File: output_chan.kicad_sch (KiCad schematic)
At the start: 12 parts, among them U5 MAX14917AFM+

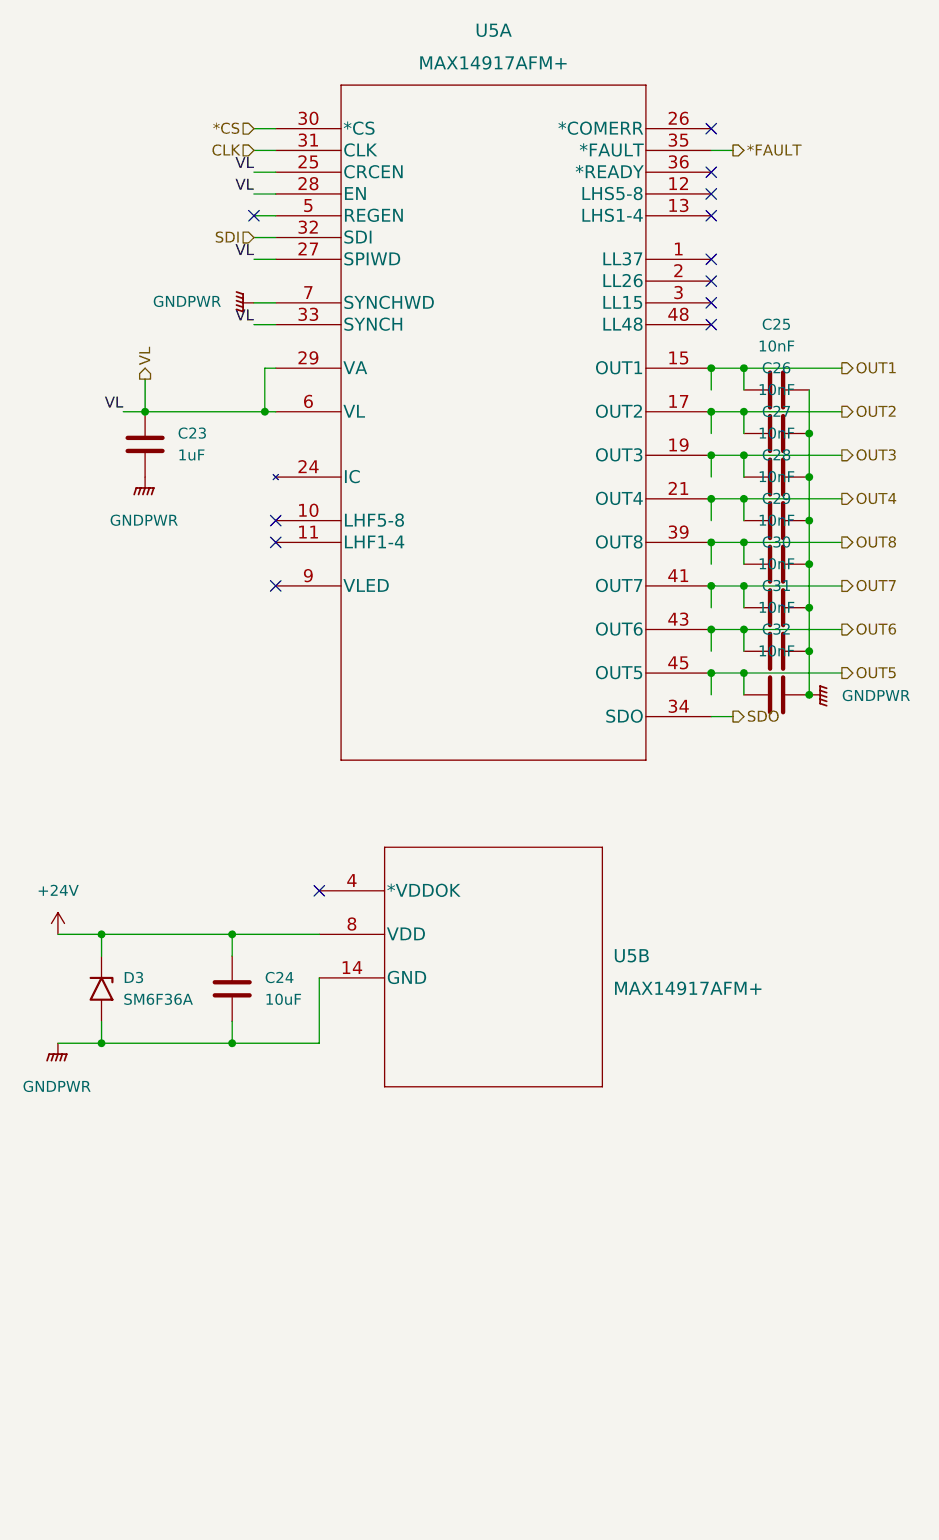
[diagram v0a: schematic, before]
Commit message: Common power stage for field IO
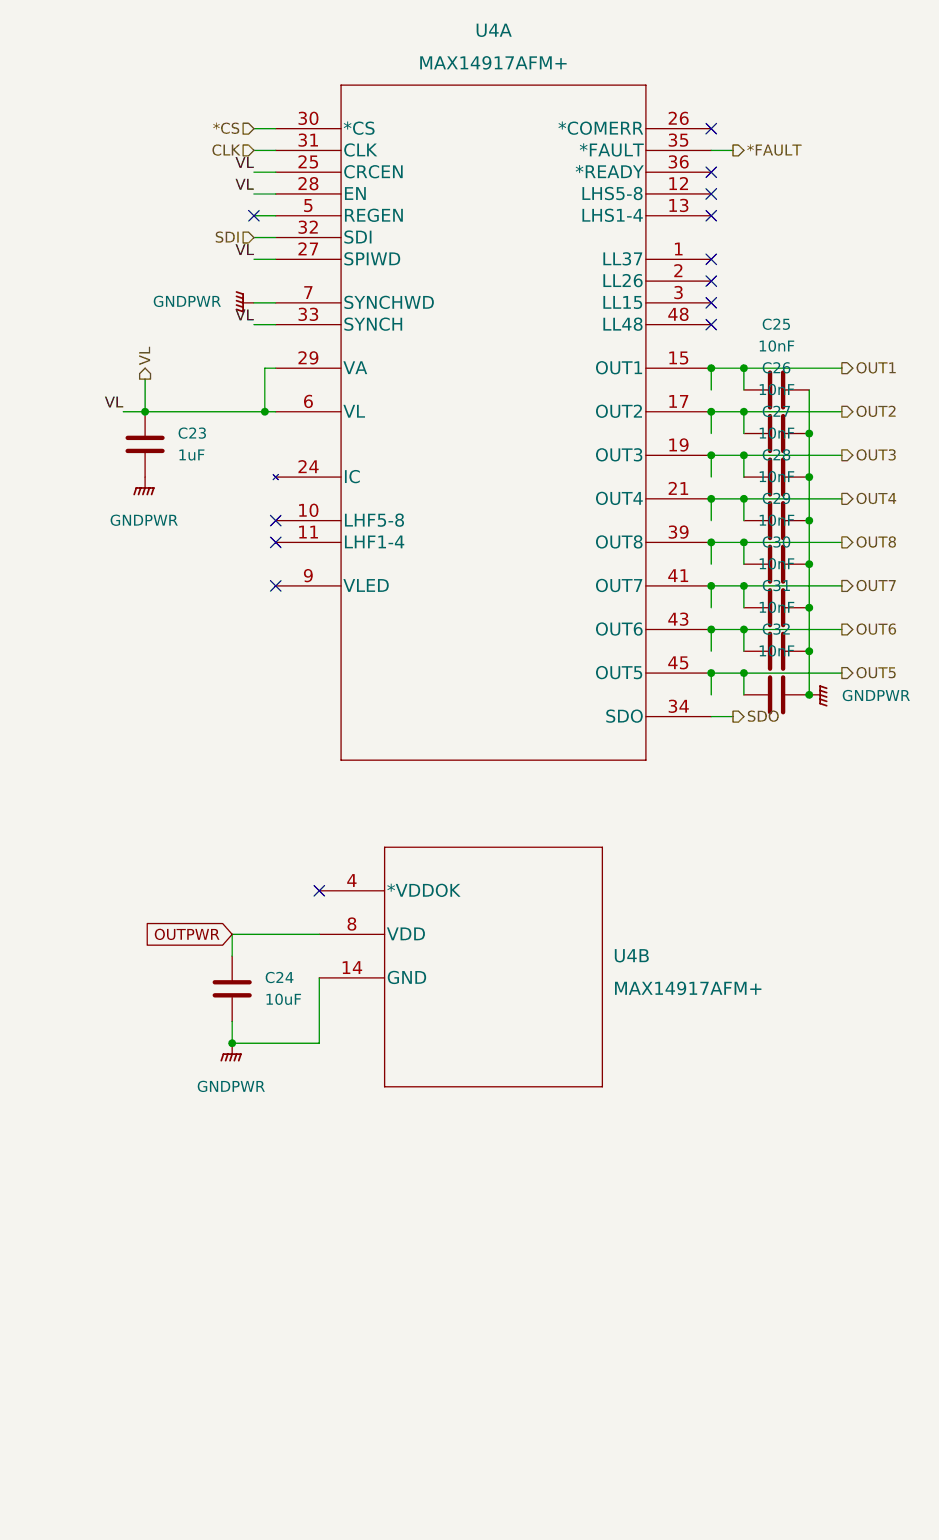
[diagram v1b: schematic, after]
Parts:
- removed D3: SM6F36A, Diode_SMD:D_SMB, symbol Diode:SM6T36A
- renumbered U5 to U4
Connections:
- net +24V renamed OUTPWR
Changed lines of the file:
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@@
   (junction (at 177.8 81.28) (diameter 0) (color 0 0 0 0)
   )
-  (junction (at 106.68 149.86) (diameter 0) (color 0 0 0 0)
-  )
-  (junction (at 121.92 137.16) (diameter 0) (color 0 0 0 0)
-  )
   (junction (at 177.8 96.52) (diameter 0) (color 0 0 0 0)
   )
@@
   (junction (at 189.23 88.9) (diameter 0) (color 0 0 0 0)
   )
-  (junction (at 106.68 137.16) (diameter 0) (color 0 0 0 0)
-  )
   (junction (at 181.61 91.44) (diameter 0) (color 0 0 0 0)
   )
@@
   (junction (at 125.73 76.2) (diameter 0) (color 0 0 0 0)
   )
+  (junction (at 189.23 93.98) (diameter 0) (color 0 0 0 0)
+  )
+  (junction (at 111.76 76.2) (diameter 0) (color 0 0 0 0)
+  )
+  (junction (at 181.61 106.68) (diameter 0) (color 0 0 0 0)
+  )
+  (junction (at 177.8 71.12) (diameter 0) (color 0 0 0 0)
+  )
   (junction (at 121.92 149.86) (diameter 0) (color 0 0 0 0)
-  )
-  (junction (at 189.23 93.98) (diameter 0) (color 0 0 0 0)
-  )
-  (junction (at 111.76 76.2) (diameter 0) (color 0 0 0 0)
-  )
-  (junction (at 181.61 106.68) (diameter 0) (color 0 0 0 0)
-  )
-  (junction (at 177.8 71.12) (diameter 0) (color 0 0 0 0)
   )
   (junction (at 181.61 86.36) (diameter 0) (color 0 0 0 0)
@@
     (stroke (width 0) (type default) (color 0 0 0 0))
   )
-  (wire (pts (xy 106.68 149.86) (xy 121.92 149.86))
-    (stroke (width 0) (type default) (color 0 0 0 0))
-  )
   (wire (pts (xy 125.73 71.12) (xy 125.73 76.2))
     (stroke (width 0) (type default) (color 0 0 0 0))
@@
     (stroke (width 0) (type default) (color 0 0 0 0))
   )
+  (wire (pts (xy 181.61 71.12) (xy 181.61 73.66))
+    (stroke (width 0) (type default) (color 0 0 0 0))
+  )
+  (wire (pts (xy 177.8 91.44) (xy 177.8 93.98))
+    (stroke (width 0) (type default) (color 0 0 0 0))
+  )
   (wire (pts (xy 121.92 149.86) (xy 132.08 149.86))
     (stroke (width 0) (type default) (color 0 0 0 0))
   )
-  (wire (pts (xy 181.61 71.12) (xy 181.61 73.66))
-    (stroke (width 0) (type default) (color 0 0 0 0))
-  )
-  (wire (pts (xy 177.8 91.44) (xy 177.8 93.98))
-    (stroke (width 0) (type default) (color 0 0 0 0))
-  )
   (wire (pts (xy 189.23 104.14) (xy 189.23 109.22))
     (stroke (width 0) (type default) (color 0 0 0 0))
   )
-  (wire (pts (xy 101.6 149.86) (xy 106.68 149.86))
-    (stroke (width 0) (type default) (color 0 0 0 0))
-  )
   (wire (pts (xy 181.61 91.44) (xy 193.04 91.44))
     (stroke (width 0) (type default) (color 0 0 0 0))
@@
     (stroke (width 0) (type default) (color 0 0 0 0))
   )
-  (wire (pts (xy 106.68 147.32) (xy 106.68 149.86))
-    (stroke (width 0) (type default) (color 0 0 0 0))
-  )
   (wire (pts (xy 127 71.12) (xy 125.73 71.12))
     (stroke (width 0) (type default) (color 0 0 0 0))
@@
     (stroke (width 0) (type default) (color 0 0 0 0))
   )
-  (wire (pts (xy 106.68 137.16) (xy 121.92 137.16))
-    (stroke (width 0) (type default) (color 0 0 0 0))
-  )
   (wire (pts (xy 111.76 76.2) (xy 125.73 76.2))
     (stroke (width 0) (type default) (color 0 0 0 0))
   )
   (wire (pts (xy 121.92 137.16) (xy 121.92 139.7))
-    (stroke (width 0) (type default) (color 0 0 0 0))
-  )
-  (wire (pts (xy 101.6 137.16) (xy 106.68 137.16))
-    (stroke (width 0) (type default) (color 0 0 0 0))
-  )
-  (wire (pts (xy 106.68 137.16) (xy 106.68 139.7))
     (stroke (width 0) (type default) (color 0 0 0 0))
   )
@@
     (effects (font (size 1.27 1.27)) (justify right bottom))
   )
+  (global_label "OUTPWR" (shape input) (at 121.92 137.16 180) (fields_autoplaced)
+    (effects (font (size 1.27 1.27)) (justify right))
+    (property "Intersheet References" "${INTERSHEET_REFS}" (id 0) (at 111.8869 137.0806 0)
+      (effects (font (size 1.27 1.27)) (justify right) hide)
+    )
+  )
   (hierarchical_label "OUT5" (shape output) (at 193.04 106.68 0)
     (effects (font (size 1.27 1.27)) (justify left))
@@
   (symbol (lib_id "power:GNDPWR") (at 189.23 109.22 90) (unit 1)
     (in_bom yes) (on_board yes) (fields_autoplaced)
-    (property "Reference" "#PWR020" (id 0) (at 194.31 109.22 0)
+    (property "Reference" "#PWR023" (id 0) (at 194.31 109.22 0)
       (effects (font (size 1.27 1.27)) hide)
     )
@@
   (symbol (lib_id "power:GNDPWR") (at 111.76 83.82 0) (unit 1)
     (in_bom yes) (on_board yes) (fields_autoplaced)
-    (property "Reference" "#PWR019" (id 0) (at 111.76 88.9 0)
+    (property "Reference" "#PWR020" (id 0) (at 111.76 88.9 0)
       (effects (font (size 1.27 1.27)) hide)
     )
@@
   (symbol (lib_id "Maxim industrial IO:MAX14917AFM+") (at 127 43.18 0) (unit 1)
     (in_bom yes) (on_board yes) (fields_autoplaced)
-    (property "Reference" "U5" (id 0) (at 152.4 31.75 0)
+    (property "Reference" "U4" (id 0) (at 152.4 31.75 0)
       (effects (font (size 1.524 1.524)))
     )
@@
   (symbol (lib_id "power:GNDPWR") (at 124.46 63.5 270) (unit 1)
     (in_bom yes) (on_board yes) (fields_autoplaced)
-    (property "Reference" "#PWR0111" (id 0) (at 119.38 63.5 0)
+    (property "Reference" "#PWR022" (id 0) (at 119.38 63.5 0)
       (effects (font (size 1.27 1.27)) hide)
     )
@@
   (symbol (lib_id "Maxim industrial IO:MAX14917AFM+") (at 132.08 132.08 0) (unit 2)
     (in_bom yes) (on_board yes) (fields_autoplaced)
-    (property "Reference" "U5" (id 0) (at 166.37 139.7 0)
+    (property "Reference" "U4" (id 0) (at 166.37 139.7 0)
       (effects (font (size 1.524 1.524)) (justify left))
     )
@@
     (pin "2")
   )
-  (symbol (lib_id "power:+24V") (at 101.6 137.16 0) (unit 1)
-    (in_bom yes) (on_board yes)
-    (property "Reference" "#PWR017" (id 0) (at 101.6 140.97 0)
-      (effects (font (size 1.27 1.27)) hide)
-    )
-    (property "Value" "+24V" (id 1) (at 101.6 132.08 0))
-    (property "Footprint" "" (id 2) (at 101.6 137.16 0)
-      (effects (font (size 1.27 1.27)) hide)
-    )
-    (property "Datasheet" "" (id 3) (at 101.6 137.16 0)
-      (effects (font (size 1.27 1.27)) hide)
-    )
-    (pin "1")
-  )
   (symbol (lib_id "Device:C") (at 185.42 73.66 90) (unit 1)
     (in_bom yes) (on_board yes) (fields_autoplaced)
@@
     (pin "2")
   )
-  (symbol (lib_id "power:GNDPWR") (at 101.6 149.86 0) (unit 1)
-    (in_bom yes) (on_board yes) (fields_autoplaced)
-    (property "Reference" "#PWR018" (id 0) (at 101.6 154.94 0)
-      (effects (font (size 1.27 1.27)) hide)
-    )
-    (property "Value" "GNDPWR" (id 1) (at 101.473 154.94 0))
-    (property "Footprint" "" (id 2) (at 101.6 151.13 0)
-      (effects (font (size 1.27 1.27)) hide)
-    )
-    (property "Datasheet" "" (id 3) (at 101.6 151.13 0)
+  (symbol (lib_id "power:GNDPWR") (at 121.92 149.86 0) (unit 1)
+    (in_bom yes) (on_board yes) (fields_autoplaced)
+    (property "Reference" "#PWR021" (id 0) (at 121.92 154.94 0)
+      (effects (font (size 1.27 1.27)) hide)
+    )
+    (property "Value" "GNDPWR" (id 1) (at 121.793 154.94 0))
+    (property "Footprint" "" (id 2) (at 121.92 151.13 0)
+      (effects (font (size 1.27 1.27)) hide)
+    )
+    (property "Datasheet" "" (id 3) (at 121.92 151.13 0)
       (effects (font (size 1.27 1.27)) hide)
     )
@@
       (effects (font (size 1.27 1.27)) hide)
     )
-    (pin "1")
-    (pin "2")
-  )
-  (symbol (lib_id "Diode:SM6T36A") (at 106.68 143.51 270) (unit 1)
-    (in_bom yes) (on_board yes) (fields_autoplaced)
-    (property "Reference" "D3" (id 0) (at 109.22 142.2399 90)
-      (effects (font (size 1.27 1.27)) (justify left))
-    )
-    (property "Value" "SM6F36A" (id 1) (at 109.22 144.7799 90)
-      (effects (font (size 1.27 1.27)) (justify left))
-    )
-    (property "Footprint" "Diode_SMD:D_SMB" (id 2) (at 101.6 143.51 0)
-      (effects (font (size 1.27 1.27)) hide)
-    )
-    (property "Datasheet" "https://www.st.com/resource/en/datasheet/sm6t.pdf" (id 3) (at 106.68 142.24 0)
-      (effects (font (size 1.27 1.27)) hide)
-    )

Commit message: fix DRC errors
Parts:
- renumbered C23 to C11, C24 to C12, C25 to C13, C26 to C14, C27 to C15, C28 to C16, C29 to C17, C30 to C18, C31 to C19, C32 to C20, U4 to U2
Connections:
- net GNDPWR: now also U2.5 (REGEN); no longer U2.14 (GND), U2.23 (GND), U2.38 (GND), U2.47 (GND)
- net OUTPWR: now also U2.25 (CRCEN); no longer U2.49 (EPAD), U2.8 (VDD)
- new net: U2.15 (OUT1), U2.16 (OUT1)
- new net: U2.17 (OUT2), U2.18 (OUT2)
- new net: U2.19 (OUT3), U2.20 (OUT3)
- new net: U2.21 (OUT4), U2.22 (OUT4)
- new net: U2.37 (VL), U2.6 (VL)
- new net: U2.39 (OUT8), U2.40 (OUT8)
- new net: U2.41 (OUT7), U2.42 (OUT7)
- new net: U2.43 (OUT6), U2.44 (OUT6)
- new net: U2.45 (OUT5), U2.46 (OUT5)
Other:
- note added: "Ajouter un LED de status ?"
- note added: "Deja une PullUp"
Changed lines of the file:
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@@
     (stroke (width 0) (type default) (color 0 0 0 0))
+  )
+  (text "Deja une PullUp" (at 105.41 67.31 0)
+    (effects (font (size 1.27 1.27) italic) (justify left bottom))
+  )
+  (text "Ajouter un LED de status ?" (at 104.14 133.35 0)
+    (effects (font (size 1.27 1.27) italic) (justify left bottom))
   )
   (label "VL" (at 109.22 76.2 180)
@@
     (effects (font (size 1.27 1.27)) (justify right))
   )
-  (symbol (lib_id "power:GNDPWR") (at 189.23 109.22 90) (unit 1)
+  (symbol (lib_id "power:GNDPWR") (at 189.23 109.22 90)
     (in_bom yes) (on_board yes) (fields_autoplaced)
     (property "Reference" "#PWR023" (id 0) (at 194.31 109.22 0)
@@
     (pin "1")
   )
-  (symbol (lib_id "Device:C") (at 111.76 80.01 0) (unit 1)
-    (in_bom yes) (on_board yes) (fields_autoplaced)
-    (property "Reference" "C23" (id 0) (at 115.57 78.7399 0)
+  (symbol (lib_id "Device:C") (at 111.76 80.01 0)
+    (in_bom yes) (on_board yes) (fields_autoplaced)
+    (property "Reference" "C11" (id 0) (at 115.57 78.7399 0)
       (effects (font (size 1.27 1.27)) (justify left))
     )
@@
     (pin "2")
   )
-  (symbol (lib_id "power:GNDPWR") (at 111.76 83.82 0) (unit 1)
+  (symbol (lib_id "power:GNDPWR") (at 111.76 83.82 0)
     (in_bom yes) (on_board yes) (fields_autoplaced)
     (property "Reference" "#PWR020" (id 0) (at 111.76 88.9 0)
@@
     (pin "1")
   )
-  (symbol (lib_id "Maxim industrial IO:MAX14917AFM+") (at 127 43.18 0) (unit 1)
-    (in_bom yes) (on_board yes) (fields_autoplaced)
-    (property "Reference" "U4" (id 0) (at 152.4 31.75 0)
+  (symbol (lib_id "Maxim industrial IO:MAX14917AFM+") (at 127 43.18 0)
+    (in_bom yes) (on_board yes) (fields_autoplaced)
+    (property "Reference" "U2" (id 0) (at 152.4 31.75 0)
       (effects (font (size 1.524 1.524)))
     )
@@
     (pin "7")
     (pin "9")
-    (pin "14")
-    (pin "23")
-    (pin "38")
-    (pin "4")
-    (pin "47")
-    (pin "49")
-    (pin "8")
-  )
-  (symbol (lib_id "Device:C") (at 185.42 83.82 90) (unit 1)
-    (in_bom yes) (on_board yes) (fields_autoplaced)
-    (property "Reference" "C27" (id 0) (at 185.42 76.2 90))
+  )
+  (symbol (lib_id "Device:C") (at 185.42 83.82 90)
+    (in_bom yes) (on_board yes) (fields_autoplaced)
+    (property "Reference" "C15" (id 0) (at 185.42 76.2 90))
     (property "Value" "10nF" (id 1) (at 185.42 78.74 90))
     (property "Footprint" "Capacitor_SMD:C_0603_1608Metric" (id 2) (at 189.23 82.8548 0)
@@
     (pin "2")
   )
-  (symbol (lib_id "Device:C") (at 185.42 88.9 90) (unit 1)
-    (in_bom yes) (on_board yes) (fields_autoplaced)
-    (property "Reference" "C28" (id 0) (at 185.42 81.28 90))
+  (symbol (lib_id "Device:C") (at 185.42 88.9 90)
+    (in_bom yes) (on_board yes) (fields_autoplaced)
+    (property "Reference" "C16" (id 0) (at 185.42 81.28 90))
     (property "Value" "10nF" (id 1) (at 185.42 83.82 90))
     (property "Footprint" "Capacitor_SMD:C_0603_1608Metric" (id 2) (at 189.23 87.9348 0)
@@
     (pin "2")
   )
-  (symbol (lib_id "Device:C") (at 185.42 78.74 90) (unit 1)
-    (in_bom yes) (on_board yes) (fields_autoplaced)
-    (property "Reference" "C26" (id 0) (at 185.42 71.12 90))
+  (symbol (lib_id "Device:C") (at 185.42 78.74 90)
+    (in_bom yes) (on_board yes) (fields_autoplaced)
+    (property "Reference" "C14" (id 0) (at 185.42 71.12 90))
     (property "Value" "10nF" (id 1) (at 185.42 73.66 90))
     (property "Footprint" "Capacitor_SMD:C_0603_1608Metric" (id 2) (at 189.23 77.7748 0)
@@
     (pin "2")
   )
-  (symbol (lib_id "Device:C") (at 185.42 104.14 90) (unit 1)
-    (in_bom yes) (on_board yes) (fields_autoplaced)
-    (property "Reference" "C31" (id 0) (at 185.42 96.52 90))
+  (symbol (lib_id "Device:C") (at 185.42 104.14 90)
+    (in_bom yes) (on_board yes) (fields_autoplaced)
+    (property "Reference" "C19" (id 0) (at 185.42 96.52 90))
     (property "Value" "10nF" (id 1) (at 185.42 99.06 90))
     (property "Footprint" "Capacitor_SMD:C_0603_1608Metric" (id 2) (at 189.23 103.1748 0)
@@
     (pin "2")
   )
-  (symbol (lib_id "power:GNDPWR") (at 124.46 63.5 270) (unit 1)
+  (symbol (lib_id "power:GNDPWR") (at 124.46 63.5 270)
     (in_bom yes) (on_board yes) (fields_autoplaced)
     (property "Reference" "#PWR022" (id 0) (at 119.38 63.5 0)
@@
     (pin "1")
   )
-  (symbol (lib_id "Maxim industrial IO:MAX14917AFM+") (at 132.08 132.08 0) (unit 2)
-    (in_bom yes) (on_board yes) (fields_autoplaced)
-    (property "Reference" "U4" (id 0) (at 166.37 139.7 0)
+  (symbol (lib_id "Maxim industrial IO:MAX14917AFM+") (at 132.08 132.08 0)
+    (in_bom yes) (on_board yes) (fields_autoplaced)
+    (property "Reference" "U2" (id 0) (at 166.37 139.7 0)
       (effects (font (size 1.524 1.524)) (justify left))
     )
@@
     (pin "7")
     (pin "9")
-    (pin "14")
-    (pin "23")
-    (pin "38")
-    (pin "4")
-    (pin "47")
-    (pin "49")
-    (pin "8")
-  )
-  (symbol (lib_id "Device:C") (at 185.42 93.98 90) (unit 1)
-    (in_bom yes) (on_board yes) (fields_autoplaced)
-    (property "Reference" "C29" (id 0) (at 185.42 86.36 90))
+  )
+  (symbol (lib_id "Device:C") (at 185.42 93.98 90)
+    (in_bom yes) (on_board yes) (fields_autoplaced)
+    (property "Reference" "C17" (id 0) (at 185.42 86.36 90))
     (property "Value" "10nF" (id 1) (at 185.42 88.9 90))
     (property "Footprint" "Capacitor_SMD:C_0603_1608Metric" (id 2) (at 189.23 93.0148 0)
@@
     (pin "2")
   )
-  (symbol (lib_id "Device:C") (at 185.42 73.66 90) (unit 1)
-    (in_bom yes) (on_board yes) (fields_autoplaced)
-    (property "Reference" "C25" (id 0) (at 185.42 66.04 90))
+  (symbol (lib_id "Device:C") (at 185.42 73.66 90)
+    (in_bom yes) (on_board yes) (fields_autoplaced)
+    (property "Reference" "C13" (id 0) (at 185.42 66.04 90))
     (property "Value" "10nF" (id 1) (at 185.42 68.58 90))
     (property "Footprint" "Capacitor_SMD:C_0603_1608Metric" (id 2) (at 189.23 72.6948 0)
@@
     (pin "2")
   )
-  (symbol (lib_id "Device:C") (at 185.42 99.06 90) (unit 1)
-    (in_bom yes) (on_board yes) (fields_autoplaced)
-    (property "Reference" "C30" (id 0) (at 185.42 91.44 90))
+  (symbol (lib_id "Device:C") (at 185.42 99.06 90)
+    (in_bom yes) (on_board yes) (fields_autoplaced)
+    (property "Reference" "C18" (id 0) (at 185.42 91.44 90))
     (property "Value" "10nF" (id 1) (at 185.42 93.98 90))
     (property "Footprint" "Capacitor_SMD:C_0603_1608Metric" (id 2) (at 189.23 98.0948 0)
@@
     (pin "2")
   )
-  (symbol (lib_id "power:GNDPWR") (at 121.92 149.86 0) (unit 1)
+  (symbol (lib_id "power:GNDPWR") (at 121.92 149.86 0)
     (in_bom yes) (on_board yes) (fields_autoplaced)
     (property "Reference" "#PWR021" (id 0) (at 121.92 154.94 0)
@@
     (pin "1")
   )
-  (symbol (lib_id "Device:C") (at 121.92 143.51 0) (unit 1)
-    (in_bom yes) (on_board yes) (fields_autoplaced)
-    (property "Reference" "C24" (id 0) (at 125.73 142.2399 0)
+  (symbol (lib_id "Device:C") (at 121.92 143.51 0)
+    (in_bom yes) (on_board yes) (fields_autoplaced)
+    (property "Reference" "C12" (id 0) (at 125.73 142.2399 0)
       (effects (font (size 1.27 1.27)) (justify left))
     )
@@
     (pin "2")
   )
-  (symbol (lib_id "Device:C") (at 185.42 109.22 90) (unit 1)
-    (in_bom yes) (on_board yes) (fields_autoplaced)
-    (property "Reference" "C32" (id 0) (at 185.42 101.6 90))
+  (symbol (lib_id "Device:C") (at 185.42 109.22 90)
+    (in_bom yes) (on_board yes) (fields_autoplaced)
+    (property "Reference" "C20" (id 0) (at 185.42 101.6 90))
     (property "Value" "10nF" (id 1) (at 185.42 104.14 90))
     (property "Footprint" "Capacitor_SMD:C_0603_1608Metric" (id 2) (at 189.23 108.2548 0)
